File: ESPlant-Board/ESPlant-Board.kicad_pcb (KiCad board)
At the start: 2 copper layers, 22 x 127 mm, 36 parts, among them J1 Conn_01x05, U1 ESP32-C6-MINI-1/U, U3 Reset, U4 Boot, U5 Temp/Humid-Sensor, U6 Light sensor, U7 AMS1117-3_3, U8 MK-12C02-G025

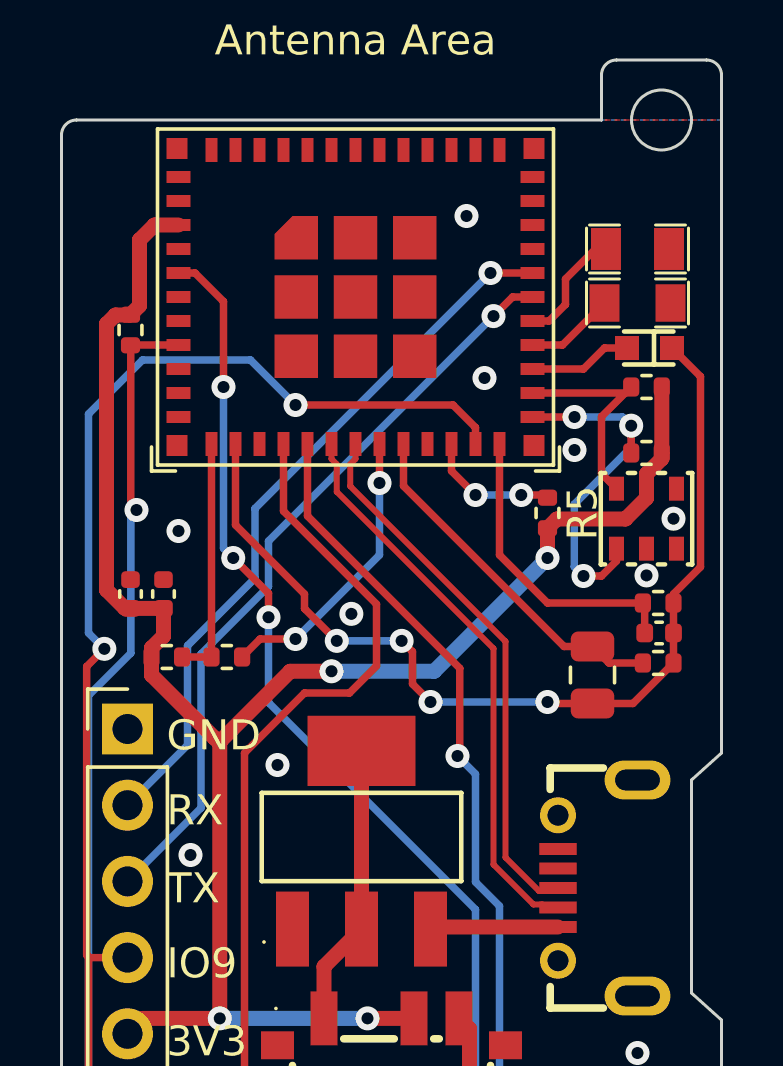
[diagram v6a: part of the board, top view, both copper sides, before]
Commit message: Board: Can now differentiate between usb or battery connected
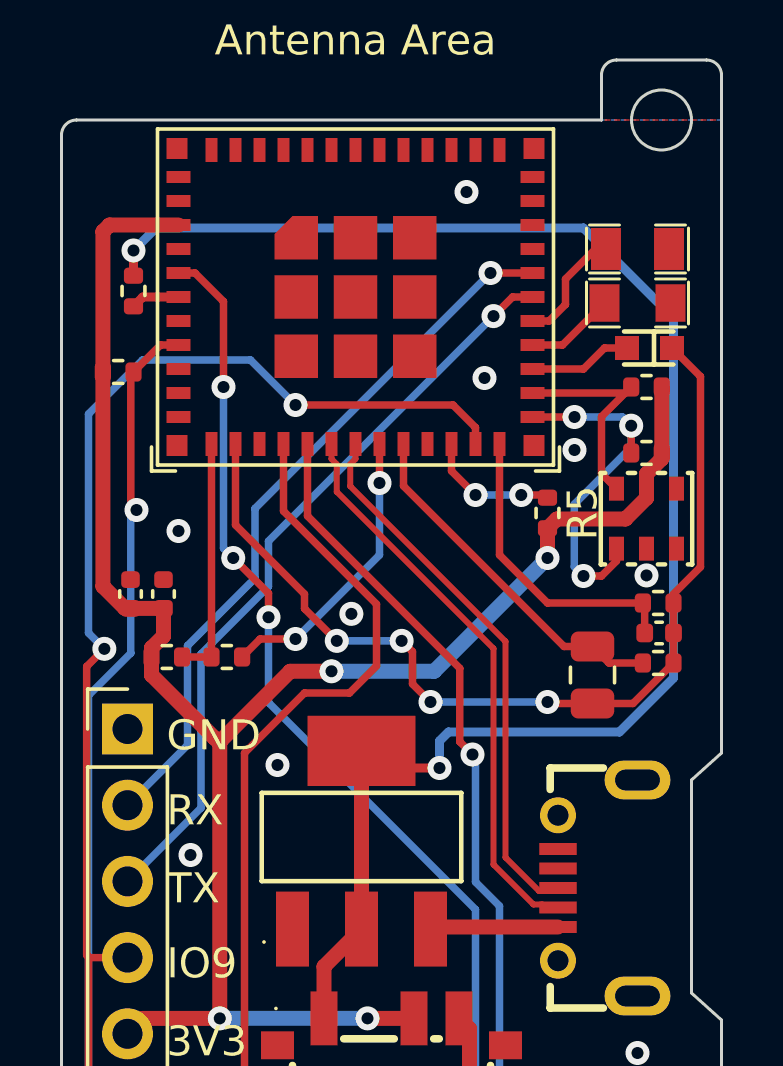
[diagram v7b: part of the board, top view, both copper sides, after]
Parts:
- added R7: 10k, Resistor_SMD:R_0402_1005Metric, F.Cu at (102.4, 105.7)
- moved R9 1.46 mm to (101.9, 108.4), turned to 0 degrees
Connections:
- U1 pad 6: unconnected-(U1-GPIO3/ADC1_CH3-Pad6) -> Net-(U1-GPIO3/ADC1_CH3)
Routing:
- net /USB: track 9.43 -> 54.2 mm, vias 0 -> 2
- net Net-(U1-GPIO3/ADC1_CH3): track 0.00 -> 1.63 mm
- net +3V3: track 62.7 -> 63.4 mm
- net /EN: track 56.0 -> 55.5 mm
- net GND: vias 14 -> 13
